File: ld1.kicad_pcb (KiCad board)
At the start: 2 copper layers, 62 x 81 mm, 42 parts, among them J1 ENCODER, J2 PROG, J3 MISC, J4 POWER, J5 5V, J6 GND, J7 3V3, J8 GPS+OLED, SW3 KLS7-KL-02-N-0-0, U1 E22-400M30S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

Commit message: Fixed pinsocket connector, fixed missing connectors footprints
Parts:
- J4: footprint Connector_PinSocket_2.54mm:PinSocket_1x03_P2.54mm_Vertical -> Connector_PinHeader_2.54mm:PinHeader_1x03_P2.54mm_Vertical
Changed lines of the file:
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@@
 		)
 	)
-	(footprint "Connector_PinSocket_2.54mm:PinSocket_1x03_P2.54mm_Vertical"
+	(footprint "Connector_PinHeader_2.54mm:PinHeader_1x03_P2.54mm_Vertical"
 		(layer "B.Cu")
 		(at 80 80.51)
-		(descr "Through hole straight socket strip, 1x03, 2.54mm pitch, single row (from Kicad 4.0.7), script generated")
-		(tags "Through hole socket strip THT 1x03 2.54mm single row")
+		(descr "Through hole straight pin header, 1x03, 2.54mm pitch, single row")
+		(tags "Through hole pin header THT 1x03 2.54mm single row")
 		(property "Reference" "J4"
-			(at 0 2.77 360)
+			(at 0 2.33 0)
 			(layer "B.SilkS")
 			(hide yes)
@@
 		)
 		(property "Value" "POWER"
-			(at 0 -7.85 360)
-			(layer "B.Fab")
-			(effects
-				(font
-					(size 1 1)
-					(thickness 0.15)
-				)
-				(justify mirror)
-			)
-		)
-		(property "Footprint" "Connector_PinSocket_2.54mm:PinSocket_1x03_P2.54mm_Vertical"
+			(at 0 -7.41 0)
+			(layer "B.Fab")
+			(effects
+				(font
+					(size 1 1)
+					(thickness 0.15)
+				)
+				(justify mirror)
+			)
+		)
+		(property "Footprint" "Connector_PinHeader_2.54mm:PinHeader_1x03_P2.54mm_Vertical"
 			(at 0 0 180)
 			(unlocked yes)
@@
 		)
 		(fp_line
+			(start -1.33 1.33)
+			(end -1.33 0)
+			(stroke
+				(width 0.12)
+				(type solid)
+			)
+			(layer "B.SilkS")
+		)
+		(fp_line
+			(start 0 1.33)
+			(end -1.33 1.33)
+			(stroke
+				(width 0.12)
+				(type solid)
+			)
+			(layer "B.SilkS")
+		)
+		(fp_line
 			(start 1.33 -6.41)
 			(end -1.33 -6.41)
@@
 		)
 		(fp_line
-			(start 1.33 0)
-			(end 1.33 1.33)
-			(stroke
-				(width 0.12)
-				(type solid)
-			)
-			(layer "B.SilkS")
-		)
-		(fp_line
-			(start 1.33 1.33)
-			(end 0 1.33)
-			(stroke
-				(width 0.12)
-				(type solid)
-			)
-			(layer "B.SilkS")
-		)
-		(fp_line
 			(start -1.8 -6.85)
-			(end 1.75 -6.85)
+			(end -1.8 1.8)
 			(stroke
 				(width 0.05)
@@
 		(fp_line
 			(start -1.8 1.8)
+			(end 1.8 1.8)
+			(stroke
+				(width 0.05)
+				(type solid)
+			)
+			(layer "B.CrtYd")
+		)
+		(fp_line
+			(start 1.8 -6.85)
 			(end -1.8 -6.85)
 			(stroke
@@
 		)
 		(fp_line
-			(start 1.75 -6.85)
-			(end 1.75 1.8)
-			(stroke
-				(width 0.05)
-				(type solid)
-			)
-			(layer "B.CrtYd")
-		)
-		(fp_line
-			(start 1.75 1.8)
-			(end -1.8 1.8)
+			(start 1.8 1.8)
+			(end 1.8 -6.85)
 			(stroke
 				(width 0.05)
@@
 		)
 		(fp_line
-			(start -1.27 1.27)
+			(start -1.27 0.635)
 			(end -1.27 -6.35)
 			(stroke
@@
 		)
 		(fp_line
-			(start 0.635 1.27)
-			(end -1.27 1.27)
+			(start -0.635 1.27)
+			(end -1.27 0.635)
 			(stroke
 				(width 0.1)
@@
 		(fp_line
 			(start 1.27 -6.35)
-			(end 1.27 0.635)
-			(stroke
-				(width 0.1)
-				(type solid)
-			)
-			(layer "B.Fab")
-		)
-		(fp_line
-			(start 1.27 0.635)
-			(end 0.635 1.27)
+			(end 1.27 1.27)
+			(stroke
+				(width 0.1)
+				(type solid)
+			)
+			(layer "B.Fab")
+		)
+		(fp_line
+			(start 1.27 1.27)
+			(end -0.635 1.27)
 			(stroke
 				(width 0.1)
@@
 			(pintype "passive")
 		)
-		(model "${KICAD8_3DMODEL_DIR}/Connector_PinSocket_2.54mm.3dshapes/PinSocket_1x03_P2.54mm_Vertical.wrl"
+		(model "${KICAD8_3DMODEL_DIR}/Connector_PinHeader_2.54mm.3dshapes/PinHeader_1x03_P2.54mm_Vertical.wrl"
 			(offset
 				(xyz 0 0 0)
@@
 		)
 		(fp_text user "${REFERENCE}"
-			(at 0 -1.27 -90)
-			(layer "B.Fab")
-			(effects
+			(at 0 -1.27 270)
+			(layer "B.Fab")
+			(effects

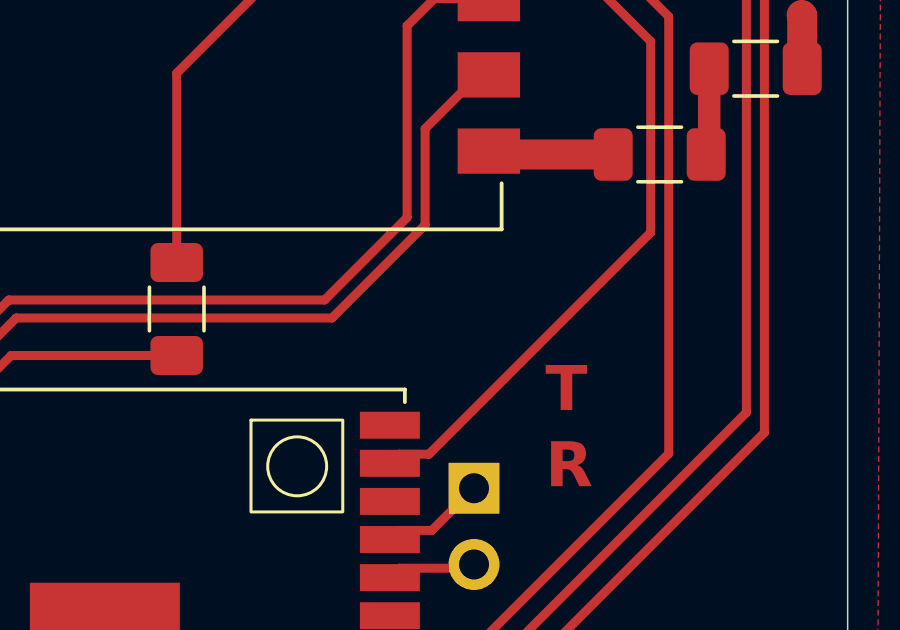
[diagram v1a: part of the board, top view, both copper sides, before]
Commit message: Added GND pin for better return current path when using underlying board
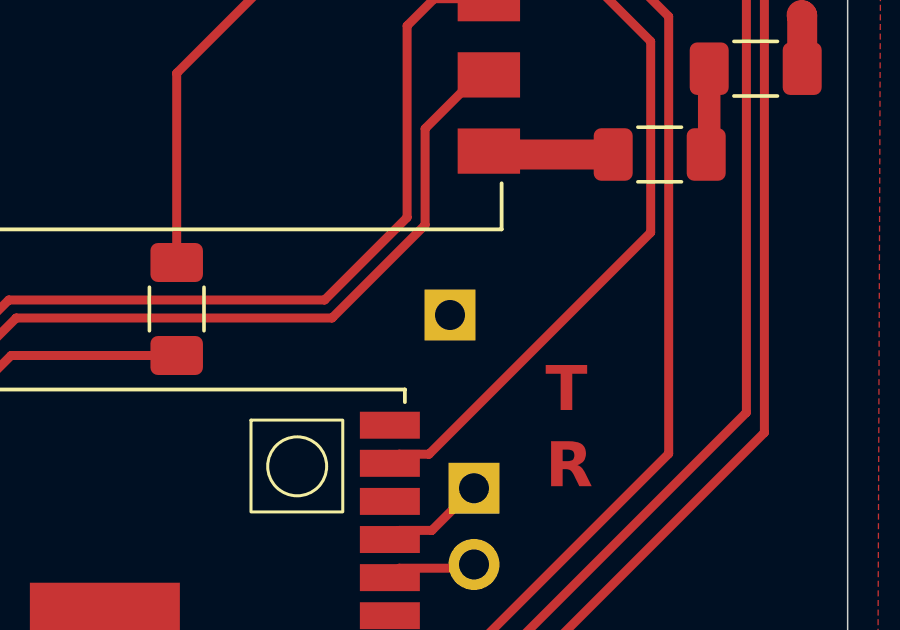
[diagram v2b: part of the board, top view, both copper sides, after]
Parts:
- added J9: GND, Connector_PinHeader_2.54mm:PinHeader_1x01_P2.54mm_Vertical, B.Cu at (119.2, 85.3)
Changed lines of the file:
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@@
+		)
+	)
+	(footprint "Connector_PinHeader_2.54mm:PinHeader_1x01_P2.54mm_Vertical"
+		(layer "B.Cu")
+		(at 119.2 85.35 180)
+		(descr "Through hole straight pin header, 1x01, 2.54mm pitch, single row")
+		(tags "Through hole pin header THT 1x01 2.54mm single row")
+		(property "Reference" "J9"
+			(at 0 2.33 180)
+			(layer "B.SilkS")
+			(effects
+				(font
+					(size 1 1)
+					(thickness 0.15)
+				)
+				(justify mirror)
+			)
+		)
+		(property "Value" "GND"
+			(at 0 -2.33 180)
+			(layer "B.Fab")
+			(effects
+				(font
+					(size 1 1)
+					(thickness 0.15)
+				)
+				(justify mirror)
+			)
+		)
+		(property "Footprint" "Connector_PinHeader_2.54mm:PinHeader_1x01_P2.54mm_Vertical"
+			(at 0 0 0)
+			(unlocked yes)
+			(layer "B.Fab")
+			(hide yes)
+			(effects
+				(font
+					(size 1.27 1.27)
+				)
+				(justify mirror)
+			)
+		)
+		(property "Datasheet" ""
+			(at 0 0 0)
+			(unlocked yes)
+			(layer "B.Fab")
+			(hide yes)
+			(effects
+				(font
+					(size 1.27 1.27)
+				)
+				(justify mirror)
+			)
+		)
+		(property "Description" "Generic connector, single row, 01x01, script generated"
+			(at 0 0 0)
+			(unlocked yes)
+			(layer "B.Fab")
+			(hide yes)
+			(effects
+				(font
+					(size 1.27 1.27)
+				)
+				(justify mirror)
+			)
+		)
+		(property ki_fp_filters "Connector*:*_1x??_*")
+		(sheetname "Root")
+		(sheetfile "ld1.kicad_sch")
+		(zone_connect 2)
+		(attr through_hole)
+		(fp_line
+			(start 1.33 -1.27)
+			(end -1.33 -1.27)
+			(stroke
+				(width 0.12)
+				(type solid)
+			)
+			(layer "B.SilkS")
+		)
+		(fp_line
+			(start 1.33 -1.33)
+			(end 1.33 -1.27)
+			(stroke
+				(width 0.12)
+				(type solid)
+			)
+			(layer "B.SilkS")
+		)
+		(fp_line
+			(start 1.33 -1.33)
+			(end -1.33 -1.33)
+			(stroke
+				(width 0.12)
+				(type solid)
+			)
+			(layer "B.SilkS")
+		)
+		(fp_line
+			(start 0 1.33)
+			(end -1.33 1.33)
+			(stroke
+				(width 0.12)
+				(type solid)
+			)
+			(layer "B.SilkS")
+		)
+		(fp_line
+			(start -1.33 1.33)
+			(end -1.33 0)
+			(stroke
+				(width 0.12)
+				(type solid)
+			)
+			(layer "B.SilkS")
+		)
+		(fp_line
+			(start -1.33 -1.33)
+			(end -1.33 -1.27)
+			(stroke
+				(width 0.12)
+				(type solid)
+			)
+			(layer "B.SilkS")
+		)
+		(fp_line
+			(start 1.8 1.8)
+			(end 1.8 -1.8)
+			(stroke
+				(width 0.05)
+				(type solid)
+			)
+			(layer "B.CrtYd")
+		)
+		(fp_line
+			(start 1.8 -1.8)
+			(end -1.8 -1.8)
+			(stroke
+				(width 0.05)
+				(type solid)
+			)
+			(layer "B.CrtYd")
+		)
+		(fp_line
+			(start -1.8 1.8)
+			(end 1.8 1.8)
+			(stroke
+				(width 0.05)
+				(type solid)
+			)
+			(layer "B.CrtYd")
+		)
+		(fp_line
+			(start -1.8 -1.8)
+			(end -1.8 1.8)
+			(stroke
+				(width 0.05)
+				(type solid)
+			)
+			(layer "B.CrtYd")
+		)
+		(fp_line
+			(start 1.27 1.27)
+			(end -0.635 1.27)
+			(stroke
+				(width 0.1)
+				(type solid)
+			)
+			(layer "B.Fab")
+		)
+		(fp_line
+			(start 1.27 -1.27)
+			(end 1.27 1.27)
+			(stroke
+				(width 0.1)
+				(type solid)
+			)
+			(layer "B.Fab")
+		)
+		(fp_line
+			(start -0.635 1.27)
+			(end -1.27 0.635)
+			(stroke
+				(width 0.1)
+				(type solid)
+			)
+			(layer "B.Fab")
+		)
+		(fp_line
+			(start -1.27 0.635)
+			(end -1.27 -1.27)
+			(stroke
+				(width 0.1)
+				(type solid)
+			)
+			(layer "B.Fab")
+		)
+		(fp_line
+			(start -1.27 -1.27)
+			(end 1.27 -1.27)
+			(stroke
+				(width 0.1)
+				(type solid)
+			)
+			(layer "B.Fab")
+		)
+		(fp_text user "${REFERENCE}"
+			(at 0 0 -90)
+			(layer "B.Fab")
+			(effects
+				(font
+					(size 1 1)
+					(thickness 0.15)
+				)
+				(justify mirror)
+			)
+		)
+		(pad "1" thru_hole rect
+			(at 0 0 180)
+			(size 1.7 1.7)
+			(drill 1)
+			(layers "*.Cu" "*.Mask")
+			(remove_unused_layers no)
+			(net 1 "GND")
+			(pinfunction "Pin_1")
+			(pintype "passive")
+		)
+		(model "${KICAD8_3DMODEL_DIR}/Connector_PinHeader_2.54mm.3dshapes/PinHeader_1x01_P2.54mm_Vertical.wrl"
+			(offset
+				(xyz 0 0 0)
+			)
+			(scale
+				(xyz 1 1 1)
+			)
+			(rotate
+				(xyz 0 0 0)
+			)
 		)
 	)

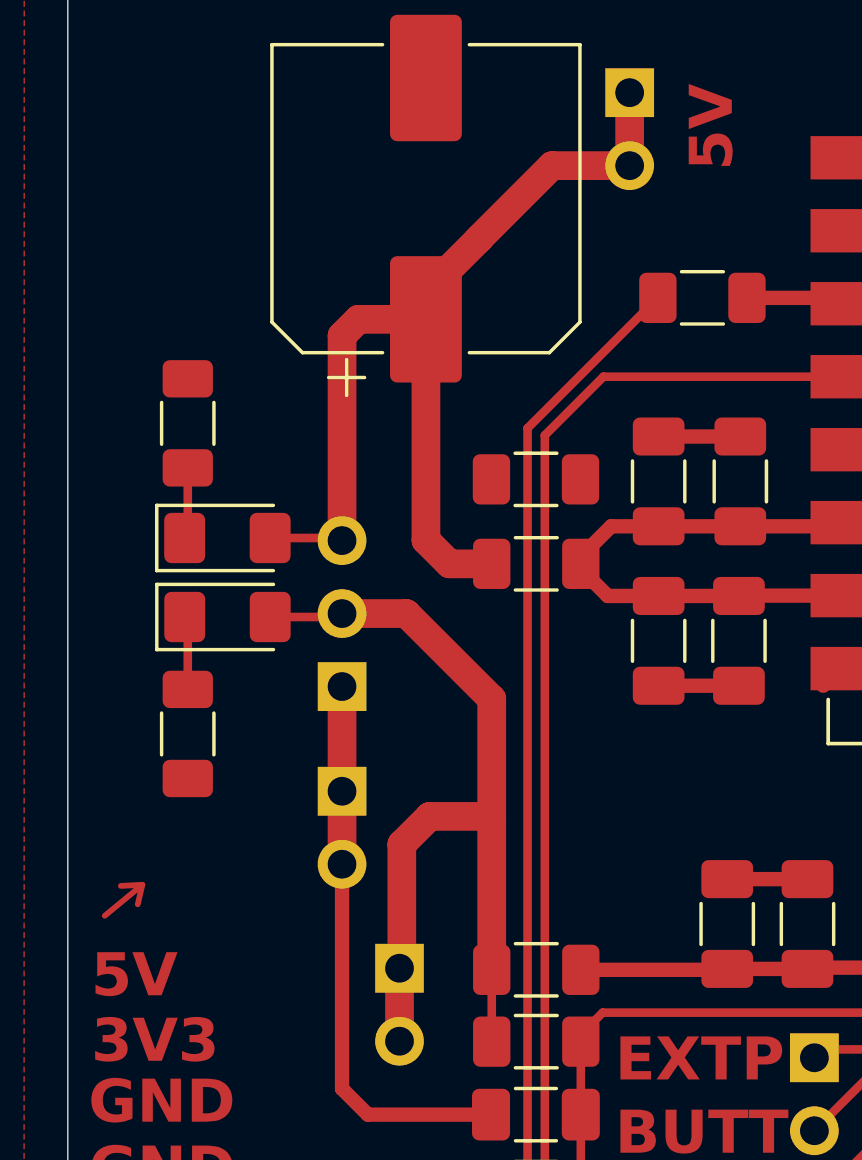
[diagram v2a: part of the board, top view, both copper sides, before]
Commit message: Added 100u caps
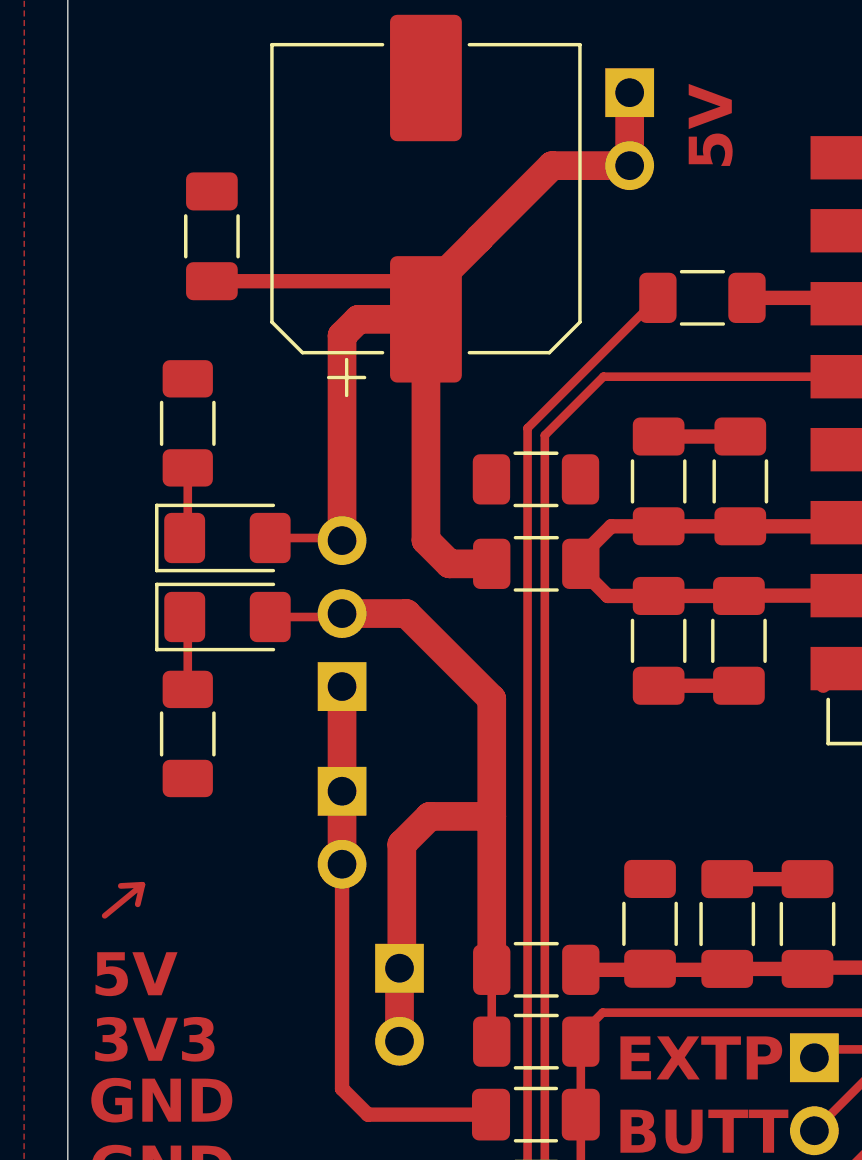
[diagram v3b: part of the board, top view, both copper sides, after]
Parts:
- added C11: 100u, Capacitor_SMD:C_1206_3216Metric_Pad1.33x1.80mm_HandSolder, F.Cu at (75.5, 64.8)
- added C12: 100u, Capacitor_SMD:C_1206_3216Metric_Pad1.33x1.80mm_HandSolder, F.Cu at (90.7, 88.8)
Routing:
- net +5V: track 54.9 -> 62.5 mm
